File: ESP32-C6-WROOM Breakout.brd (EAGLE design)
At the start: 99 x 49.5 mm, 85 parts, among them J10 HP I2C, J11 LP I2C, J2 HP I2C, J3 HP_UART, P1 LP_I2C, P10 Pwr Sw 23, P11 LiPo In, P12 Pwr Out, P14 Backup, P2 HP_I2C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

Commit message: v1.1 essentially completed
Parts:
- removed JP10, JP4: (no value), Master 2016:1X02
- removed JP12: UART Vcc, Connector:3P-2.54
- removed JP13: PS Src, Connector:3P-2.54
- removed Q4: FDN338P, Master 2016:SOT23_LONG
- added J12: UART Vcc, Connector:3P-2.54
- added R22: 22k, Master 2016:1206
- added U1: 74LVC1G3157, ESP32 Projects:DBV6
- added U4, U5: MIC2005A-1YM5, ESP32 Projects:SOT-23-5_M5_MCH-M
- added USB1: (no value), Master 2016:FCI_USB_B_SMD_LONG
- J1: value (none) -> HP I2C; device Master 2016:FCI_USB_B_SMD -> Connector:4P-2.54-80/40MIL
- J10: value HP I2C -> (none); device Connector:4P-2.54-80/40MIL -> Master 2016:1X02
- P10: device con-jst-ph:B3B-PH-K -> con-jst-ph:B2B-PH-K
- P11: value LiPo In -> Battery
- P13: value (none) -> Pwr Sw 22; device Master 2016:1X02 -> con-jst-ph:B2B-PH-K
- P5: value ADC -> ADC (ext batt)
- P9: value Pwr Sw 22 -> GPIO-B; device con-jst-ph:B2B-PH-K -> con-jst-eh:B4B-EH-A
- R15: value (none) -> 10k
- R20: value 2k2 -> 10k
- R21: value 1k -> 22k
- U2: value ESP32-C6-WROOM-1-N4 -> ESP32-C6-WROOM-1-N4LONG; device SMD Stamp Modules:MOD28_ESP32-C6-WROOM-1_EXP -> SMD Stamp Modules:MOD28_ESP32-C6-WROOM-1_LONG
- U3: value AP2112 -> RT9080-33
- moved J10 76.7 mm to (90.8, 47.0), turned to 180 degrees
- moved R20 71.5 mm to (85.1, 13.3), turned to 270 degrees
- moved R21 69.5 mm to (82.2, 13.3), turned to 270 degrees
- moved P9 50.5 mm to (45.4, 29.2), turned to 0 degrees
- moved Q2 48.3 mm to (40.0, 17.5), turned to 180 degrees
- moved P13 47.6 mm to (95.2, 15.9)
- moved J1 32.3 mm to (22.9, 11.4), turned to 90 degrees
- moved C10 12.3 mm to (83.8, 25.4)
- moved R9 12.1 mm to (32.4, 25.7)
- moved R5 11.3 mm to (73.3, 12.4)
- moved JP3 9.52 mm to (33.7, 29.2), turned to 0 degrees
- moved R15 6.39 mm to (79.4, 22.5), turned to 270 degrees
- moved P10 4.13 mm to (95.2, 36.8), turned to 270 degrees
- moved Q3 3.81 mm to (43.8, 17.5)
- moved C6 3.55 mm to (17.5, 28.6)
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- renumbered JP14 to J14, JP6 to J6, JP7 to J7, JP8 to J8, JP9 to J9
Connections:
- removed net N$14: JP13.3, P10.3
- new net ADC_EXT: P5.2, U1.3
- new net VIN_DIV: R20.1, R21.1, U1.1
- net ADC: now also U1.4; no longer P5.2, R20.1, R21.1
- net GND: now also J1.2, P10.1, P11.1, P13.1, P14.1, R15.2, R5.2, U1.2, U4.2, U5.2, USB1.GND; no longer J1.GND, J10.2, P10.2, P11.2, P14.2
- net GPIO10: now also J1.3; no longer J10.3
- net GPIO11: now also J1.4; no longer J10.4
- net GPIO12: now also USB1.D-; no longer J1.D-
- net GPIO13: now also USB1.D+; no longer J1.D+
- net GPIO15: now also R5.1, U1.6, U5.3
- net GPIO15_R: now also J10.2; no longer JP10.2
- net GPIO22: now also U4.3; no longer Q2.1, R15.2, R5.1
- net GPIO8: now also P9.3; no longer P13.1
- net GPIO9: now also P9.1; no longer P13.2
- net LP_GPIO3: now also R22.1
- net LP_GPIO4: now also P5.3, Q2.1; no longer Q3.1
- net LP_GPIO5: now also Q3.1; no longer Q4.1
- net N$12: now also Q2.3; no longer Q3.3
- net N$15: now also R21.2, U5.5; no longer JP5.2, P10.1, Q1.3
- net N$2: now also P11.2; no longer P11.1
- net N$3: now also USB1.VCC; no longer J1.VCC
- net N$4: now also P14.2; no longer P14.1
- net N$5: now also JP5.2, P10.2, Q1.3; no longer JP13.2, JP5.1, Q1.2, R8.2
- net N$7: now also Q3.3; no longer Q4.3
- net N$8: now also J10.1; no longer JP10.1
- net PWR_SW_22: now also J12.1, P13.2, U4.5; no longer JP12.1, JP4.2, P9.1, Q2.3
- net UART_VCC: now also J12.2; no longer JP12.2
- net VCC: now also J1.1, J12.3, JP5.1, P9.4, Q1.2, R22.2, R8.2, U1.5, U4.1; no longer J10.1, JP12.3, JP13.1, JP4.1, P5.3, Q4.2, R5.2
- net VIN: now also U5.1; no longer R21.2
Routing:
- net ADC: track 173.5 -> 40.2 mm
- net VIN: track 58.6 -> 147.0 mm, vias 1 -> 2
- net GPIO15: track 4.98 -> 49.3 mm, vias 0 -> 2
- net LP_GPIO4: track 72.7 -> 115.8 mm, vias 3 -> 4
- net GND: track 12.5 -> 30.3 mm, vias 6 -> 11
- net GPIO9: track 35.2 -> 50.0 mm
- net N$5: track 23.0 -> 10.0 mm
- net ADC_EXT: track 0.00 -> 12.9 mm
- net GPIO8: track 24.1 -> 31.9 mm
- net VIN_DIV: track 0.00 -> 7.75 mm
- net LP_GPIO3: track 87.1 -> 94.9 mm
- net N$15: track 9.19 -> 3.70 mm
- net N$14: track 4.88 -> 0.00 mm
- net PWR_SW_22: track 20.4 -> 24.4 mm
- net UART_VCC: track 41.6 -> 45.1 mm
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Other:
- board text added: "ESP32-C6 Prototyper Adam Cooper 2025 Version 1.1"
- board text added: "MIC2005A"
- board text removed: "Cut trace if using ADC input"
- board text removed: "ESP32-C6 Prototyper Adam Cooper 2025 Version 1.0"
- board text removed: "Ext"

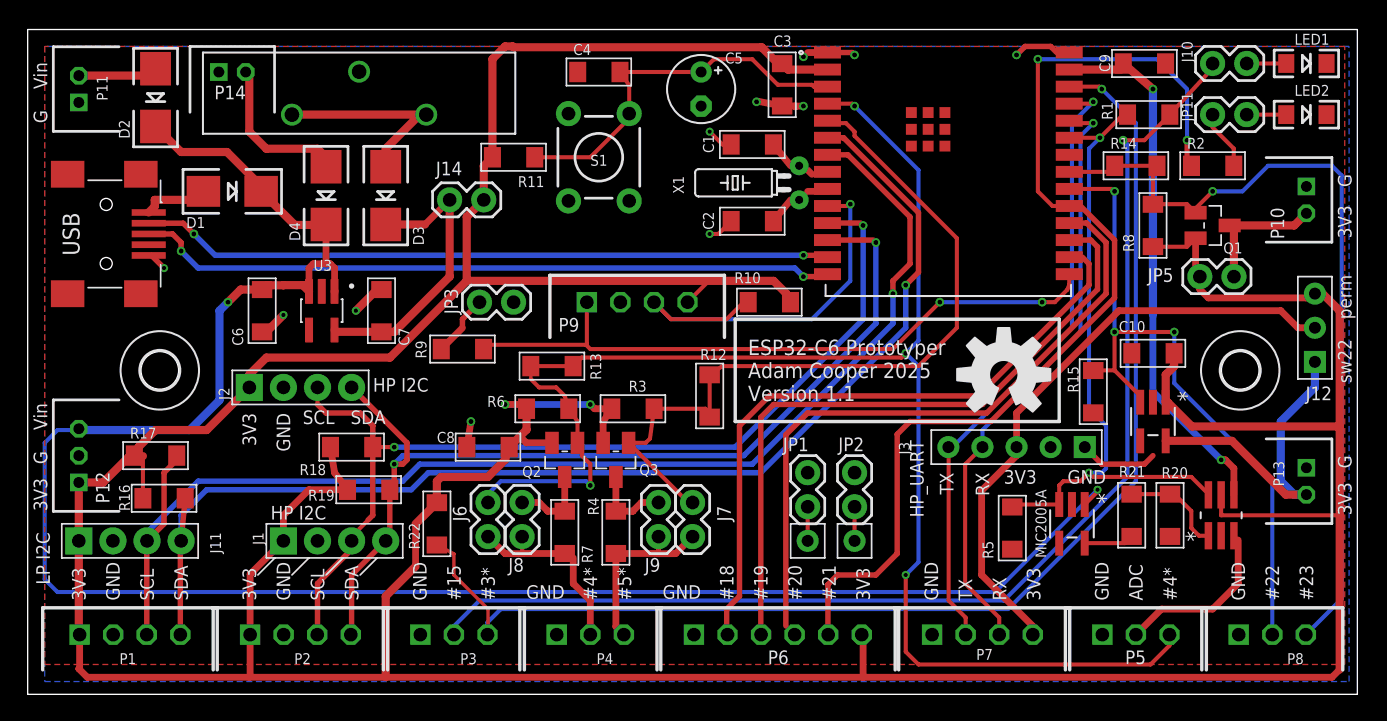
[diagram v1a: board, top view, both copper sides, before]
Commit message: prepared for panelisation process
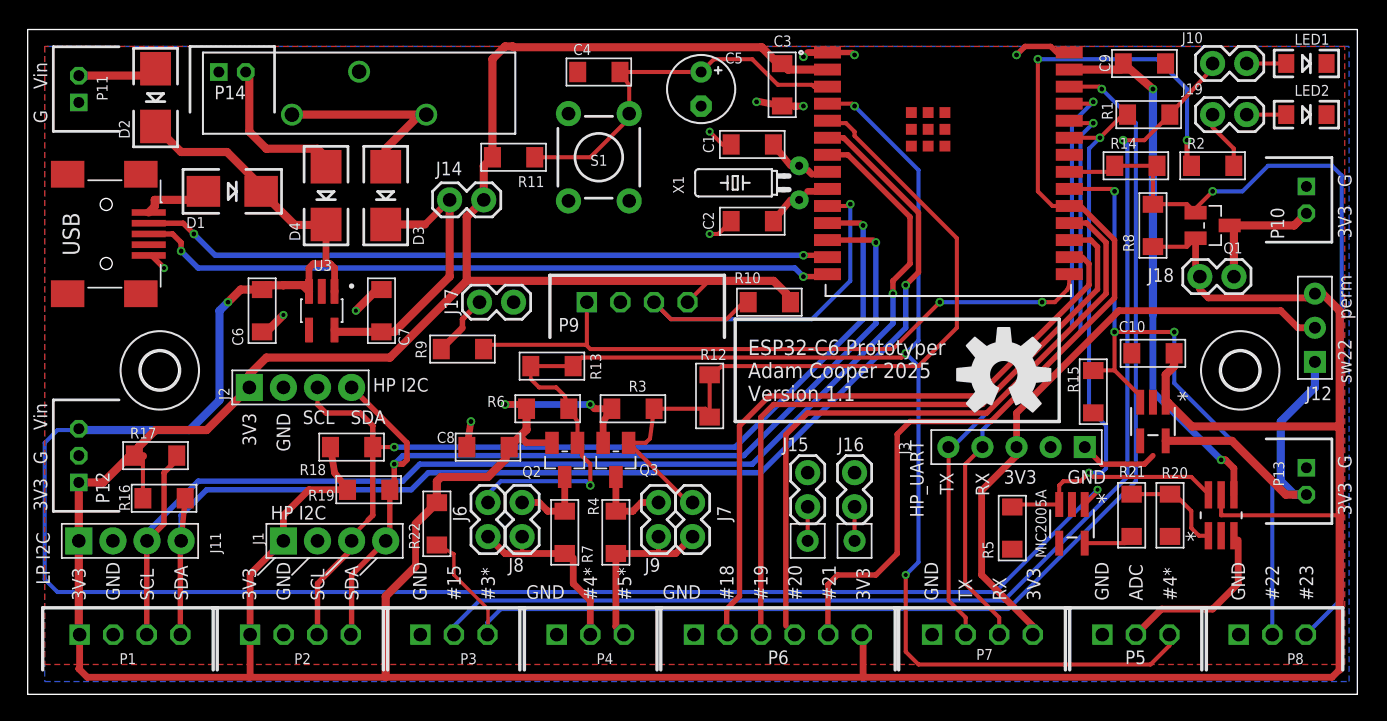
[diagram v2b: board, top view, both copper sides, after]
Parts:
- renumbered JP1 to J15, JP11 to J19, JP2 to J16, JP3 to J17, JP5 to J18
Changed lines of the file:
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@@
 <grid distance="0.05" unitdist="inch" unit="inch" style="lines" multiple="1" display="yes" altdistance="0.0125" altunitdist="inch" altunit="inch"/>
 <layers>
-<layer number="1" name="Top" color="4" fill="1" visible="no" active="yes"/>
-<layer number="16" name="Bottom" color="1" fill="1" visible="no" active="yes"/>
+<layer number="1" name="Top" color="4" fill="1" visible="yes" active="yes"/>
+<layer number="16" name="Bottom" color="1" fill="1" visible="yes" active="yes"/>
 <layer number="17" name="Pads" color="2" fill="1" visible="yes" active="yes"/>
-<layer number="18" name="Vias" color="2" fill="1" visible="no" active="yes"/>
+<layer number="18" name="Vias" color="2" fill="1" visible="yes" active="yes"/>
 <layer number="19" name="Unrouted" color="6" fill="1" visible="yes" active="yes"/>
 <layer number="20" name="Dimension" color="15" fill="1" visible="yes" active="yes"/>
@@
 <layer number="37" name="tTest" color="7" fill="1" visible="no" active="yes"/>
 <layer number="38" name="bTest" color="7" fill="1" visible="no" active="yes"/>
-<layer number="39" name="tKeepout" color="4" fill="11" visible="no" active="yes"/>
-<layer number="40" name="bKeepout" color="1" fill="11" visible="no" active="yes"/>
-<layer number="41" name="tRestrict" color="4" fill="10" visible="no" active="yes"/>
-<layer number="42" name="bRestrict" color="1" fill="10" visible="no" active="yes"/>
+<layer number="39" name="tKeepout" color="4" fill="11" visible="yes" active="yes"/>
+<layer number="40" name="bKeepout" color="1" fill="11" visible="yes" active="yes"/>
+<layer number="41" name="tRestrict" color="4" fill="10" visible="yes" active="yes"/>
+<layer number="42" name="bRestrict" color="1" fill="10" visible="yes" active="yes"/>
 <layer number="43" name="vRestrict" color="2" fill="10" visible="yes" active="yes"/>
 <layer number="44" name="Drills" color="7" fill="1" visible="no" active="yes"/>
@@
 <attribute name="VALUE" x="81.5975" y="36.83" size="0.8128" layer="27" font="vector" ratio="10" rot="R270"/>
 </element>
-<element name="JP5" library="Master 2016" package="1X02" value="" x="87.3125" y="31.115" smashed="yes">
+<element name="J18" library="Master 2016" package="1X02" value="" x="87.3125" y="31.115" smashed="yes">
 <attribute name="NAME" x="83.4263" y="30.7213" size="1.016" layer="25" ratio="10"/>
 <attribute name="VALUE" x="86.0425" y="27.94" size="1.27" layer="27"/>
@@
 <attribute name="VALUE" x="91.44" y="11.1125" size="1.016" layer="27" ratio="10"/>
 </element>
-<element name="JP1" library="Master 2016" package="1X02" value="" x="58.1025" y="13.97" smashed="yes" rot="R90">
+<element name="J15" library="Master 2016" package="1X02" value="" x="58.1025" y="13.97" smashed="yes" rot="R90">
 <attribute name="NAME" x="58.1787" y="19.1262" size="1.016" layer="25" ratio="10" rot="R180"/>
 <attribute name="VALUE" x="61.2775" y="12.7" size="1.27" layer="27" rot="R90"/>
 </element>
-<element name="JP2" library="Master 2016" package="1X02" value="" x="61.595" y="13.97" smashed="yes" rot="R90">
+<element name="J16" library="Master 2016" package="1X02" value="" x="61.595" y="13.97" smashed="yes" rot="R90">
 <attribute name="NAME" x="62.3062" y="19.1262" size="1.016" layer="25" ratio="10" rot="R180"/>
 <attribute name="VALUE" x="64.77" y="12.7" size="1.27" layer="27" rot="R90"/>
@@
 <attribute name="VALUE" x="30.1625" y="33.655" size="1.27" layer="27"/>
 </element>
-<element name="JP3" library="Master 2016" package="1X02" value="BOOT" x="33.655" y="29.21" smashed="yes">
+<element name="J17" library="Master 2016" package="1X02" value="BOOT" x="33.655" y="29.21" smashed="yes">
 <attribute name="NAME" x="31.0388" y="30.2387" size="1.016" layer="25" ratio="10" rot="R270"/>
 <attribute name="VALUE" x="37.465" y="32.0675" size="1.27" layer="27" rot="R180"/>
@@
 </element>
 <element name="J10" library="Master 2016" package="1X02" value="" x="90.805" y="46.99" smashed="yes" rot="R180">
-<attribute name="NAME" x="85.9663" y="48.6537" size="0.8128" layer="25" ratio="10" rot="R270"/>
+<attribute name="NAME" x="85.9663" y="48.5013" size="0.8128" layer="25" ratio="10"/>
 <attribute name="VALUE" x="92.075" y="50.165" size="1.27" layer="27" rot="R180"/>
 </element>
@@
 <attribute name="VALUE" x="86.36" y="37.465" size="0.8128" layer="27" font="vector" ratio="10"/>
 </element>
-<element name="JP11" library="Master 2016" package="1X02" value="" x="90.805" y="43.18" smashed="yes" rot="R180">
-<attribute name="NAME" x="85.9663" y="44.8437" size="0.8128" layer="25" ratio="10" rot="R270"/>
+<element name="J19" library="Master 2016" package="1X02" value="" x="90.805" y="43.18" smashed="yes" rot="R180">
+<attribute name="NAME" x="85.9663" y="44.6913" size="0.8128" layer="25" ratio="10"/>
 <attribute name="VALUE" x="92.075" y="46.355" size="1.27" layer="27" rot="R180"/>
 </element>
@@
 <contactref element="C1" pad="1"/>
 <contactref element="C2" pad="1"/>
-<contactref element="JP1" pad="2"/>
-<contactref element="JP2" pad="2"/>
-<contactref element="JP3" pad="2"/>
+<contactref element="J15" pad="2"/>
+<contactref element="J16" pad="2"/>
+<contactref element="J17" pad="2"/>
 <contactref element="J1" pad="2"/>
 <contactref element="J11" pad="2"/>
@@
 <contactref element="R8" pad="2"/>
 <contactref element="Q1" pad="2"/>
-<contactref element="JP5" pad="1"/>
+<contactref element="J18" pad="1"/>
 <wire x1="86.995" y1="33.975" x2="86.995" y2="31.4325" width="0.508" layer="1"/>
 <wire x1="87.3125" y1="31.115" x2="86.995" y2="31.4325" width="0.508" layer="1"/>
@@
 </signal>
 <signal name="N$1">
-<contactref element="JP3" pad="1"/>
+<contactref element="J17" pad="1"/>
 <contactref element="R9" pad="1"/>
 <wire x1="33.655" y1="29.21" x2="32.385" y2="27.94" width="0.4064" layer="1"/>
@@
 <signal name="N$10">
 <contactref element="R2" pad="2"/>
-<contactref element="JP11" pad="2"/>
+<contactref element="J19" pad="2"/>
 <wire x1="89.8398" y1="40.6527" x2="88.265" y2="42.2275" width="0.3048" layer="1"/>
 <wire x1="88.265" y1="43.18" x2="88.265" y2="42.2275" width="0.3048" layer="1"/>
@@
 </signal>
 <signal name="N$11">
-<contactref element="JP11" pad="1"/>
+<contactref element="J19" pad="1"/>
 <contactref element="LED2" pad="A"/>
 <wire x1="93.75" y1="43.18" x2="90.805" y2="43.18" width="0.3048" layer="1"/>
@@
 </signal>
 <signal name="N$9">
-<contactref element="JP2" pad="1"/>
+<contactref element="J16" pad="1"/>
 <contactref element="J5" pad="P$1"/>
 <wire x1="61.595" y1="13.97" x2="61.595" y2="11.43" width="0.3048" layer="1"/>
 </signal>
 <signal name="N$16">
-<contactref element="JP1" pad="1"/>
+<contactref element="J15" pad="1"/>
 <contactref element="J4" pad="P$1"/>
 <wire x1="58.1025" y1="13.97" x2="58.1025" y2="11.43" width="0.3048" layer="1"/>
@@
 <signal name="N$5">
 <contactref element="Q1" pad="3"/>
-<contactref element="JP5" pad="2"/>
+<contactref element="J18" pad="2"/>
 <contactref element="P10" pad="2"/>
 <wire x1="89.535" y1="34.925" x2="94.345" y2="34.925" width="0.6096" layer="1"/>

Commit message: minor tweaks with no electrical effect
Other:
- board text added: "J1"
- board text added: "J12"
- board text added: "J14"
- board text added: "J15"
- board text added: "J16"
- board text added: "J17"
- board text added: "J18"
- board text added: "J19"
- board text added: "J6"
- board text added: "J7"
- board text added: "J8"
- board text added: "J9"
- board text added: "R22"
- board text added: "U1"
- board text added: "U4"
- board text added: "U5"
- board text removed: "JP1"
- board text removed: "JP10"
- board text removed: "JP11"
- board text removed: "JP12"
- board text removed: "JP13"
- board text removed: "JP14"
- board text removed: "JP2"
- board text removed: "JP3"
- board text removed: "JP4"
- board text removed: "JP5"
- board text removed: "JP6"
- board text removed: "JP7"
- board text removed: "JP8"
- board text removed: "JP9"
- board text removed: "Q4"
